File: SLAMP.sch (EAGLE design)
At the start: 59 parts, among them IC2 AT42QT1070-SSU, J1 CARA1, J2 CARA4, J3 CARA2, J4 CARA5, J5 CARA3, J6 EXTRA-D10, J7 A0, Q1 2N7002PW, U1 HC_05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

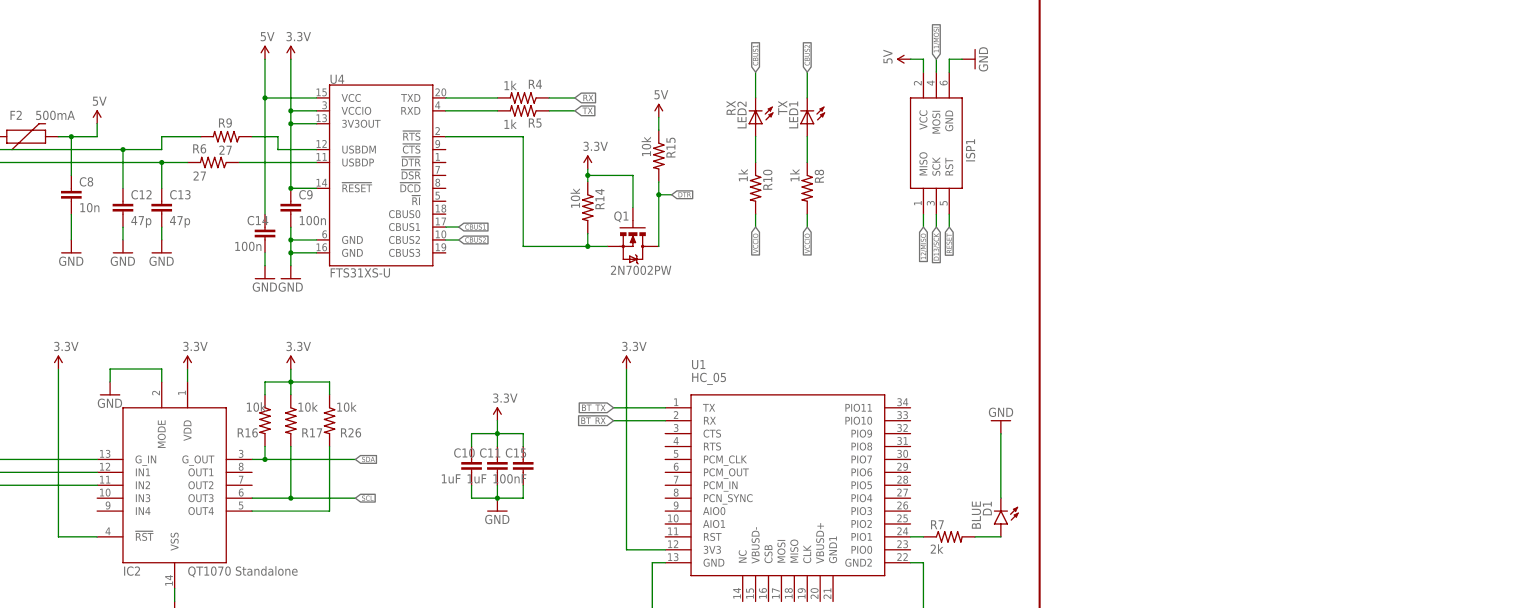
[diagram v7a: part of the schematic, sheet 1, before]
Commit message: adding system for power management
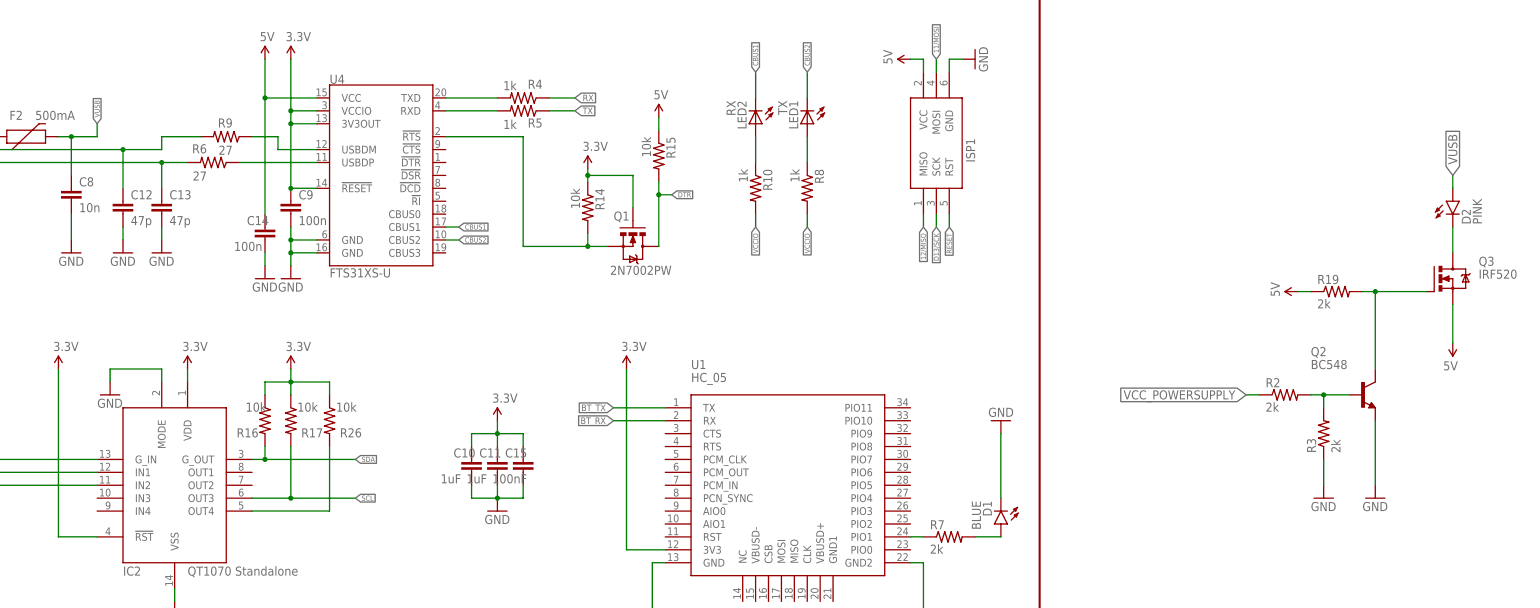
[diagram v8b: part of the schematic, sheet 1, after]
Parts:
- added D2: PINK, SparkFun-LED:LED-PINK1206
- added Q2: BC548, transistor-npn:BC548
- added Q3: IRF520, transistor-power:IRF520
- added R19, R2, R3: 2k, SparkFun-Passives:RESISTOR0805-RES
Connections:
- new net N$22: D2.C, Q3.D
- new net N$6: Q2.B, R2.2, R3.2
- new net N$7: Q2.C, Q3.G, R19.2
- new net VCC_POWERSUPPLY: R2.1
- new net VUSB: C8.1, D2.A, F2.2
- net 5V: now also Q3.S, R19.1; no longer C8.1, F2.2
- net GND: now also Q2.E, R3.1
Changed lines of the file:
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@@
 <part name="GND15" library="SparkFun-Aesthetics" deviceset="GND" device=""/>
 <part name="C9" library="SparkFun-Passives" deviceset="CAP" device="0603-CAP" value="100n"/>
-<part name="SUPPLY7" library="SparkFun-Aesthetics" deviceset="5V" device=""/>
 <part name="F2" library="SparkFun-PowerIC" deviceset="PTC" device="SMD" value="500mA"/>
 <part name="C12" library="SparkFun-Passives" deviceset="CAP" device="0603-CAP" value="47p"/>
@@
 <part name="GND2" library="SparkFun-Aesthetics" deviceset="GND" device=""/>
 <part name="SUPPLY1" library="SparkFun-Aesthetics" deviceset="5V" device=""/>
+<part name="R2" library="SparkFun-Passives" deviceset="RESISTOR" device="0805-RES" value="2k"/>
+<part name="R3" library="SparkFun-Passives" deviceset="RESISTOR" device="0805-RES" value="2k"/>
+<part name="Q2" library="transistor-npn" deviceset="BC548*" device=""/>
+<part name="Q3" library="transistor-power" deviceset="IRF520" device=""/>
+<part name="R19" library="SparkFun-Passives" deviceset="RESISTOR" device="0805-RES" value="2k"/>
+<part name="D2" library="SparkFun-LED" deviceset="LED-PINK" device="1206" value="PINK"/>
+<part name="GND3" library="SparkFun-Aesthetics" deviceset="GND" device=""/>
+<part name="GND4" library="SparkFun-Aesthetics" deviceset="GND" device=""/>
+<part name="SUPPLY2" library="SparkFun-Aesthetics" deviceset="5V" device=""/>
+<part name="SUPPLY3" library="SparkFun-Aesthetics" deviceset="5V" device=""/>
 </parts>
 <sheets>
@@
 <instance part="GND15" gate="1" x="142.24" y="-53.34"/>
 <instance part="C9" gate="G$1" x="142.24" y="-40.64"/>
-<instance part="SUPPLY7" gate="G$1" x="104.14" y="-22.86"/>
 <instance part="F2" gate="G$1" x="88.9" y="-25.4" smashed="yes">
 <attribute name="NAME" x="86.868" y="-22.098" size="1.778" layer="95"/>
@@
 <instance part="FRAME1" gate="G$1" x="40.64" y="-182.88"/>
 <instance part="FRAME1" gate="V" x="187.96" y="-182.88"/>
+<instance part="R2" gate="G$1" x="337.82" y="-76.2"/>
+<instance part="R3" gate="G$1" x="345.44" y="-83.82" rot="R90"/>
+<instance part="Q2" gate="G$1" x="353.06" y="-76.2"/>
+<instance part="Q3" gate="G$1" x="368.3" y="-53.34"/>
+<instance part="R19" gate="G$1" x="347.98" y="-55.88"/>
+<instance part="D2" gate="G$1" x="370.84" y="-38.1"/>
+<instance part="GND3" gate="1" x="345.44" y="-96.52"/>
+<instance part="GND4" gate="1" x="355.6" y="-96.52"/>
+<instance part="SUPPLY2" gate="G$1" x="340.36" y="-55.88" rot="R90"/>
+<instance part="SUPPLY3" gate="G$1" x="370.84" y="-66.04" rot="R180"/>
 </instances>
 <busses>
@@
 <wire x1="266.7" y1="-109.22" x2="266.7" y2="-119.38" width="0.1524" layer="91"/>
 </segment>
+<segment>
+<pinref part="R3" gate="G$1" pin="1"/>
+<pinref part="GND3" gate="1" pin="GND"/>
+<wire x1="345.44" y1="-88.9" x2="345.44" y2="-93.98" width="0.1524" layer="91"/>
+</segment>
+<segment>
+<pinref part="GND4" gate="1" pin="GND"/>
+<pinref part="Q2" gate="G$1" pin="E"/>
+<wire x1="355.6" y1="-93.98" x2="355.6" y2="-81.28" width="0.1524" layer="91"/>
+</segment>
 </net>
 <net name="DTR" class="0">
@@
 <net name="5V" class="0">
 <segment>
-<pinref part="F2" gate="G$1" pin="2"/>
-<pinref part="C8" gate="G$1" pin="1"/>
-<wire x1="96.52" y1="-25.4" x2="99.06" y2="-25.4" width="0.1524" layer="91"/>
-<wire x1="99.06" y1="-25.4" x2="99.06" y2="-33.02" width="0.1524" layer="91"/>
-<wire x1="99.06" y1="-25.4" x2="104.14" y2="-25.4" width="0.1524" layer="91"/>
-<junction x="99.06" y="-25.4"/>
-<wire x1="104.14" y1="-25.4" x2="104.14" y2="-22.86" width="0.1524" layer="91"/>
-<pinref part="SUPPLY7" gate="G$1" pin="5V"/>
-</segment>
-<segment>
 <pinref part="U4" gate="U$1" pin="VCC"/>
 <wire x1="147.32" y1="-17.78" x2="137.16" y2="-17.78" width="0.1524" layer="91"/>
@@
 <wire x1="266.7" y1="-12.7" x2="266.7" y2="-10.16" width="0.1524" layer="91"/>
 <wire x1="266.7" y1="-10.16" x2="264.16" y2="-10.16" width="0.1524" layer="91"/>
+</segment>
+<segment>
+<pinref part="SUPPLY2" gate="G$1" pin="5V"/>
+<pinref part="R19" gate="G$1" pin="1"/>
+<wire x1="340.36" y1="-55.88" x2="342.9" y2="-55.88" width="0.1524" layer="91"/>
+</segment>
+<segment>
+<pinref part="SUPPLY3" gate="G$1" pin="5V"/>
+<pinref part="Q3" gate="G$1" pin="S"/>
+<wire x1="370.84" y1="-66.04" x2="370.84" y2="-58.42" width="0.1524" layer="91"/>
 </segment>
 </net>
@@
 </segment>
 </net>
+<net name="VUSB" class="0">
+<segment>
+<pinref part="F2" gate="G$1" pin="2"/>
+<pinref part="C8" gate="G$1" pin="1"/>
+<wire x1="96.52" y1="-25.4" x2="99.06" y2="-25.4" width="0.1524" layer="91"/>
+<wire x1="99.06" y1="-25.4" x2="99.06" y2="-33.02" width="0.1524" layer="91"/>
+<wire x1="99.06" y1="-25.4" x2="104.14" y2="-25.4" width="0.1524" layer="91"/>
+<junction x="99.06" y="-25.4"/>
+<wire x1="104.14" y1="-25.4" x2="104.14" y2="-22.86" width="0.1524" layer="91"/>
+<label x="104.14" y="-22.86" size="1.016" layer="95" rot="R90" xref="yes"/>
+</segment>
+<segment>
+<pinref part="D2" gate="G$1" pin="A"/>
+<wire x1="370.84" y1="-35.56" x2="370.84" y2="-33.02" width="0.1524" layer="91"/>
+<label x="370.84" y="-33.02" size="1.778" layer="95" rot="R90" xref="yes"/>
+</segment>
+</net>
+<net name="N$6" class="0">
+<segment>
+<pinref part="R2" gate="G$1" pin="2"/>
+<pinref part="Q2" gate="G$1" pin="B"/>
+<wire x1="342.9" y1="-76.2" x2="345.44" y2="-76.2" width="0.1524" layer="91"/>
+<pinref part="R3" gate="G$1" pin="2"/>
+<wire x1="345.44" y1="-76.2" x2="350.52" y2="-76.2" width="0.1524" layer="91"/>
+<wire x1="345.44" y1="-78.74" x2="345.44" y2="-76.2" width="0.1524" layer="91"/>
+<junction x="345.44" y="-76.2"/>
+</segment>
+</net>
+<net name="N$7" class="0">
+<segment>
+<pinref part="Q2" gate="G$1" pin="C"/>
+<wire x1="355.6" y1="-71.12" x2="355.6" y2="-55.88" width="0.1524" layer="91"/>
+<pinref part="R19" gate="G$1" pin="2"/>
+<wire x1="355.6" y1="-55.88" x2="353.06" y2="-55.88" width="0.1524" layer="91"/>
+<pinref part="Q3" gate="G$1" pin="G"/>
+<wire x1="355.6" y1="-55.88" x2="365.76" y2="-55.88" width="0.1524" layer="91"/>
+<junction x="355.6" y="-55.88"/>
+</segment>
+</net>
+<net name="N$22" class="0">
+<segment>
+<pinref part="Q3" gate="G$1" pin="D"/>
+<pinref part="D2" gate="G$1" pin="C"/>
+<wire x1="370.84" y1="-48.26" x2="370.84" y2="-43.18" width="0.1524" layer="91"/>
+</segment>
+</net>
+<net name="VCC_POWERSUPPLY" class="0">
+<segment>
+<pinref part="R2" gate="G$1" pin="1"/>
+<wire x1="332.74" y1="-76.2" x2="330.2" y2="-76.2" width="0.1524" layer="91"/>
+<label x="330.2" y="-76.2" size="1.778" layer="95" rot="R180" xref="yes"/>
+</segment>
+</net>
